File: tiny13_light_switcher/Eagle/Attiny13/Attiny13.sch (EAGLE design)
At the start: 34 parts, among them Q1 2SA1015, Q2 2SC1815, Q3 2SA1015, U1 ATTiny13

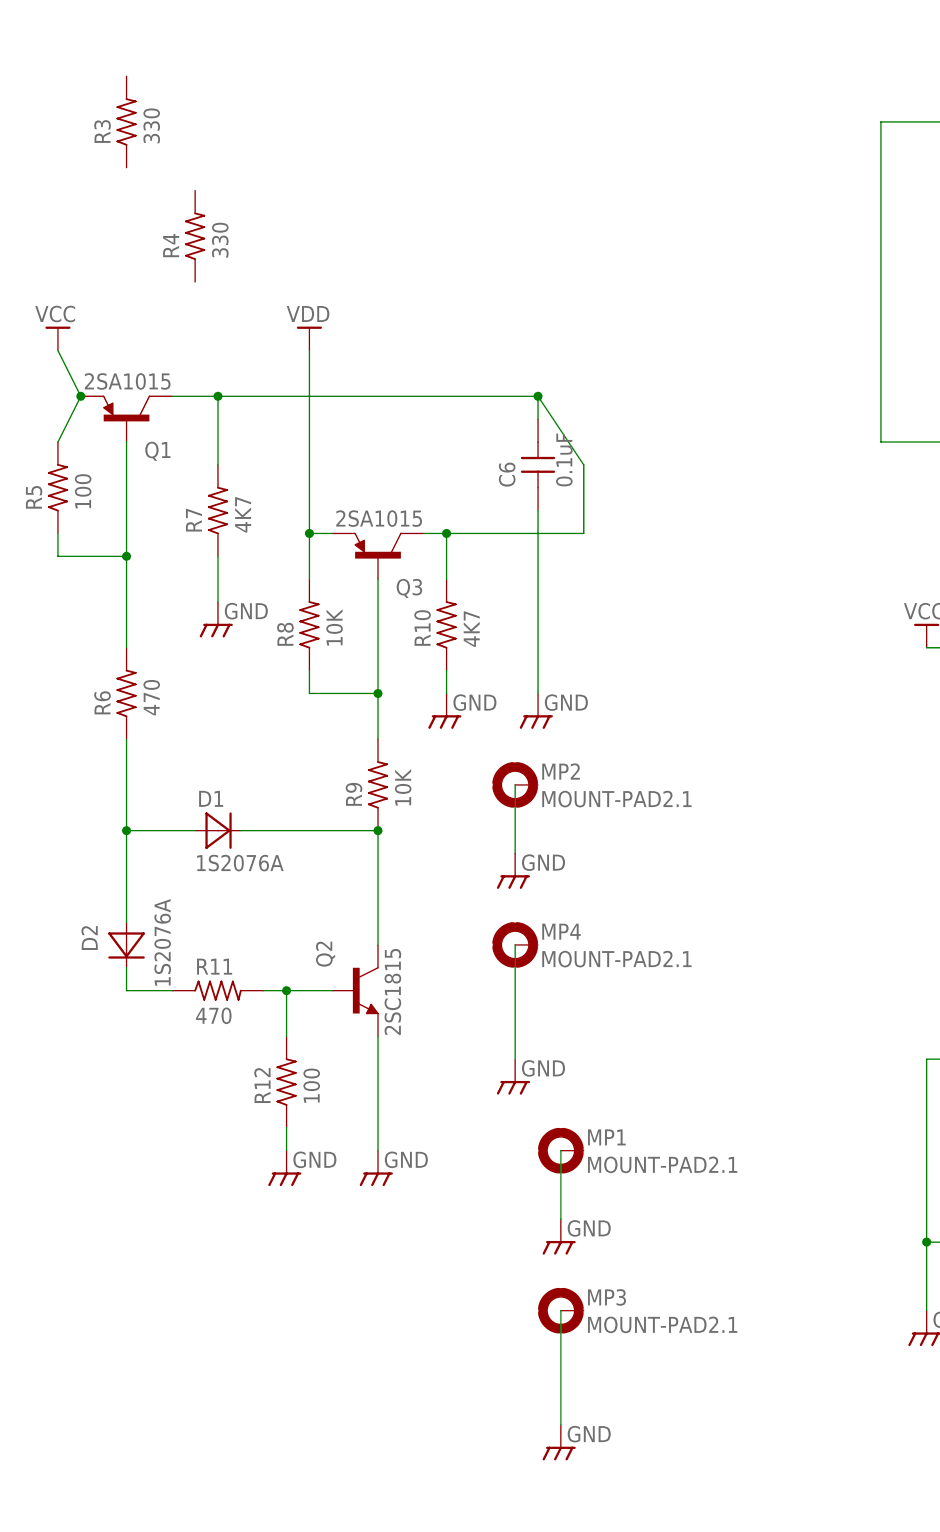
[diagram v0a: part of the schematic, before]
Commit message: Remove no use parts.
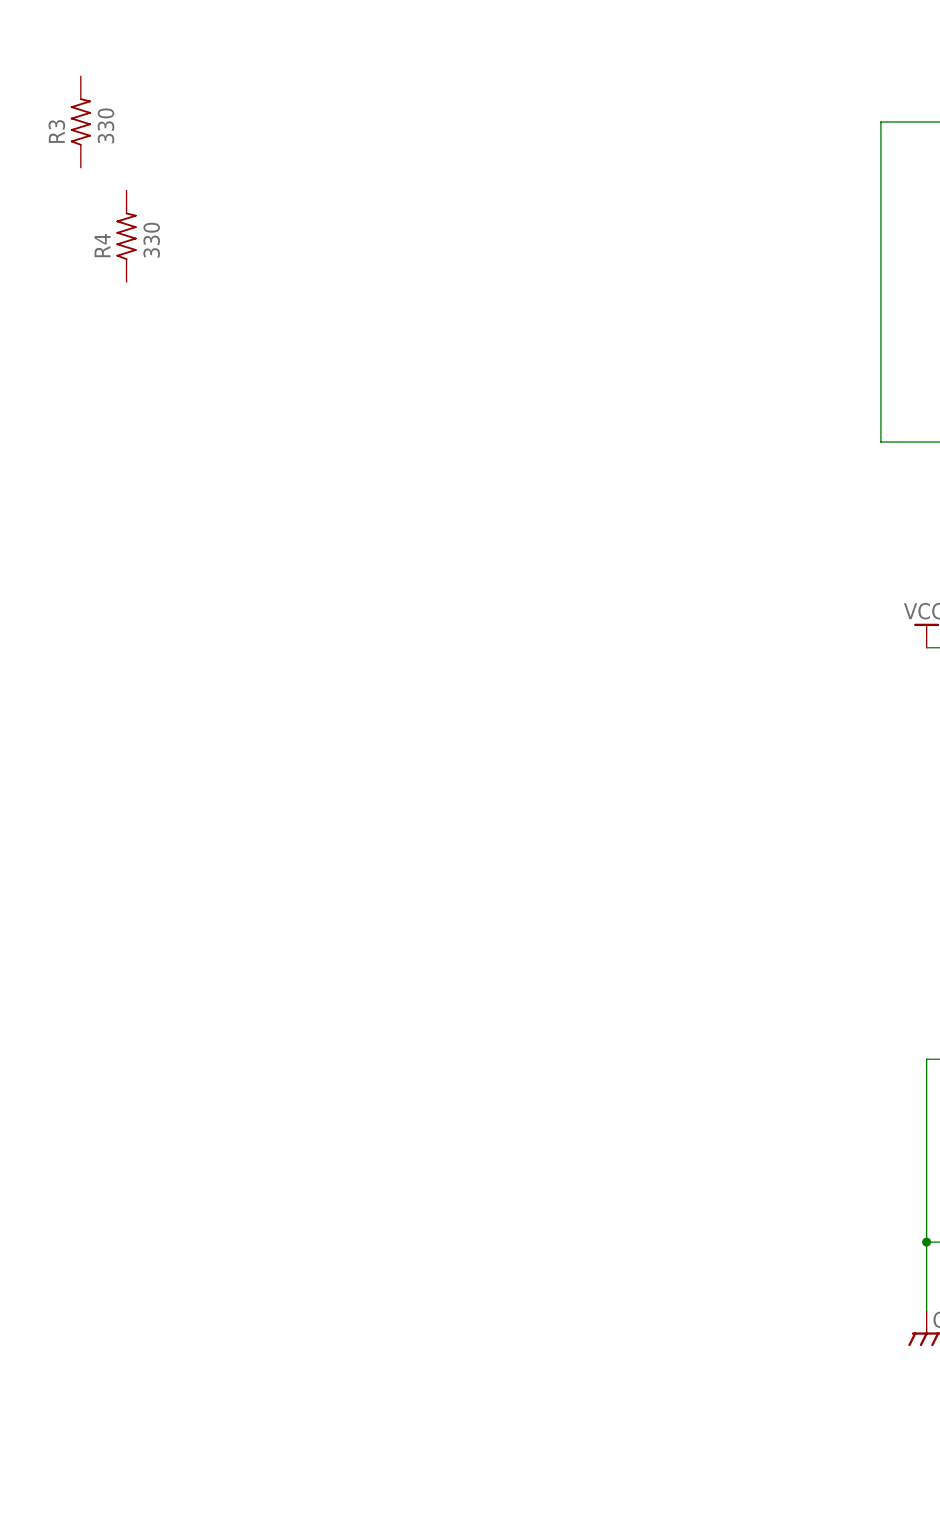
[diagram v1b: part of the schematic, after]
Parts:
- removed C6: 0.1uF, MyLib:CAPDIP_1
- removed D1, D2: 1S2076A, MyLib:DIODEGENERIC_2
- removed MP1, MP2, MP3, MP4: MOUNT-PAD2.1, MyLib:MOUNT-PAD2.1
- removed Q1, Q3: 2SA1015, MyLib:2SA1015
- removed Q2: 2SC1815, MyLib:2SC1815
- removed R10, R7: 4K7, MyLib:R0.125W_3P
- removed R11, R6: 470, MyLib:R0.125W_3P
- removed R12, R5: 100, MyLib:R0.125W_3P
- removed R8, R9: 10K, MyLib:R0.125W_3P
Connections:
- removed net N$11: Q1.B, R5.1, R6.2
- removed net N$13: Q3.B, R8.1, R9.2
- removed net N$14: Q2.B, R11.2, R12.2
- removed net N$15: D1.K, Q2.C, R9.1
- removed net N$16: D2.K, R11.1
- removed net N$17: D1.A, D2.A, R6.1
- removed net N$3: C6.2, Q1.C, Q3.C, R10.2, R7.2
- removed net VDD: Q3.E, R8.2
- net GND: no longer C6.1, MP1.MOUNT, MP2.MOUNT, MP3.MOUNT, MP4.MOUNT, Q2.E, R10.1, R12.1, R7.1
- net VCC: no longer Q1.E, R5.2
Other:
- moved on the sheet: R3, R4

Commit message: Add tiny85 writer.
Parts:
- added C1: 0.1uF, MyLib:CAPDIP_1
- added C2: 4.7uF, MyLib:CAPDIP_1
- added D1: ＳＢＭ１０４５ＶＳＳ, adafruit:SCHOTTKY-DIODEDO41
- added D2, D3: ＧＤＺＪ３．６Ｂ, diode:ZENER-DIODEDO34-7
- added ESDV_L, ESDV_R, ESDV_R2: PINHD-1X10, adafruit:PINHD-1X10
- added J1: USB_A_SMT_MALE, SparkFun-Connectors:USB_A_SMT_MALE
- added JP3: VINSEL, pinhead:PINHD-1X3
- added JP5: (no value), pinhead:PINHD-1X2
- added JP6: VSEL, pinhead:PINHD-1X3
- added JP7: Regulator, pinhead:PINHD-1X5
- added LED8, LED9: (no value), adafruit:LEDSFH480
- added R1: 68R, MyLib:R0.125W_3P
- added R5, R6: (no value), MyLib:R0.125W_3P
- added U2: ATTiny85, atmel:TINY138P3
- Q4, Q5, Q6: value (none) -> 2N7000
- R3: value 330 -> 1K5
- R4: value 330 -> 68R
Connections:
- new net +5V: C1.2, C2.2, ESDV_L.10, JP5.2, JP6.2, LED9.A, U2.VCC
- new net N$1: D1.C, J1.VBUS
- new net N$11: ESDV_R.7, ESDV_R2.7, R1.1, U2.PB4(ADC2/PCINT4)
- new net N$12: ESDV_R.5, ESDV_R2.5, U2.PB5(RESET#/ADC0/DW/PCINT5)
- new net N$13: LED9.C, R5.2
- new net N$14: LED8.C, R6.1
- new net N$15: ESDV_L.6, LED8.A, U2.PB1(MISO/AIN1/OC0B/INT0/PCINT1)
- new net N$16: ESDV_L.5, U2.PB0(MOSI/AIN0/OC0A/PCINT0)
- new net N$17: JP3.2, JP7.1, JP7.4
- new net N$18: ESDV_L.7, U2.PB2(SCK/ADC1/T0/PCINT2)
- new net N$19: D3.C, J1.D+, R1.2
- new net N$20: ESDV_R.10, ESDV_R2.10, JP3.1
- new net N$21: ESDV_R.2, ESDV_R2.2
- new net N$22: ESDV_R.3, ESDV_R2.3
- new net N$23: ESDV_R.4, ESDV_R2.4
- new net N$24: ESDV_R.8, ESDV_R2.8
- new net N$25: ESDV_L.1, JP5.1
- new net N$26: JP6.3, JP7.2, JP7.5
- new net N$3: ESDV_R.6, ESDV_R2.6, R4.1, U2.PB3(ADC3/CLKI/PCINT3)
- new net N$4: D2.C, J1.D-, R3.1, R4.2
- new net VDD: D1.A, JP3.3, JP6.1, R3.2
- net GND: now also C1.1, C2.1, D2.A, D3.A, ESDV_L.9, ESDV_R.1, ESDV_R.9, ESDV_R2.1, ESDV_R2.9, J1.GND, JP7.3, R5.1, R6.2, U2.GND
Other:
- note added: "& Espr Developer Socket"
- note added: "Attiny85 writer"
- moved on the sheet: R3, R4

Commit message: Change sub pin header to wroom02 breakout board.
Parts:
- removed ESDV_R2: PINHD-1X10, adafruit:PINHD-1X10
- removed JP5: (no value), pinhead:PINHD-1X2
- added WR02_L: WR02_L, pinhead:PINHD-1X8
- added WR02_R: WR02_R, pinhead:PINHD-1X8
- JP2: value (none) -> VDD
- LED8: value (none) -> PRG_LED
- LED9: value (none) -> PWR_LED
- R5: value (none) -> R_PWR_LED
- R6: value (none) -> R_PROG_LED
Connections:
- new net N$27: ESDV_R.3, WR02_R.3
- new net N$28: ESDV_R.4, WR02_R.4
- new net N$29: ESDV_R.8, WR02_R.8
- net +5V: now also WR02_L.1; no longer JP5.2
- net GND: now also WR02_R.1; no longer ESDV_R2.1, ESDV_R2.9
- net N$11: now also WR02_R.7; no longer ESDV_R2.7
- net N$12: now also WR02_R.5; no longer ESDV_R2.5
- net N$15: now also WR02_L.6
- net N$16: now also WR02_L.5
- net N$18: now also WR02_L.7
- net N$20: no longer ESDV_R2.10
- net N$21: now also ESDV_L.2, WR02_L.2; no longer ESDV_R.2, ESDV_R2.2
- net N$22: now also ESDV_L.3, WR02_L.3; no longer ESDV_R.3, ESDV_R2.3
- net N$23: now also ESDV_L.4, WR02_L.4; no longer ESDV_R.4, ESDV_R2.4
- net N$24: now also ESDV_L.8, WR02_L.8; no longer ESDV_R.8, ESDV_R2.8
- net N$25: now also ESDV_R.2, WR02_R.2; no longer ESDV_L.1, JP5.1
- net N$3: now also WR02_R.6; no longer ESDV_R2.6
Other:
- moved on the sheet: ESDV_L, LED8

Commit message: Add pattern diagram.
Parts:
- renumbered LED7 to LED2
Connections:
- net N$10: now also LED3.C; no longer LED5.C
- net N$5: now also LED6.C; no longer LED3.C
- net N$9: now also LED5.C; no longer LED6.C
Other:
- moved on the sheet: LED3, LED5, LED6
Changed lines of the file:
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@@
 <part name="VCC4" library="pwr" deviceset="VCC" device=""/>
 <part name="LED1" library="led" deviceset="LED" device="3MM" value="RED"/>
+<part name="LED6" library="led" deviceset="LED" device="3MM" value="RED"/>
+<part name="LED4" library="led" deviceset="LED" device="3MM" value="RED"/>
 <part name="LED3" library="led" deviceset="LED" device="3MM" value="RED"/>
-<part name="LED4" library="led" deviceset="LED" device="3MM" value="RED"/>
 <part name="LED5" library="led" deviceset="LED" device="3MM" value="RED"/>
-<part name="LED6" library="led" deviceset="LED" device="3MM" value="RED"/>
-<part name="LED7" library="led" deviceset="LED" device="3MM" value="RED"/>
+<part name="LED2" library="led" deviceset="LED" device="3MM" value="RED"/>
 <part name="J1" library="SparkFun-Connectors" deviceset="USB_A" device="_SMT_MALE"/>
 <part name="SUPPLY1" library="supply2" library_urn="urn:adsk.eagle:library:372" deviceset="GND" device=""/>
@@
 <instance part="VCC4" gate="VCC" x="119.38" y="106.68"/>
 <instance part="LED1" gate="G$1" x="149.86" y="86.36"/>
-<instance part="LED3" gate="G$1" x="160.02" y="86.36"/>
+<instance part="LED6" gate="G$1" x="160.02" y="86.36"/>
 <instance part="LED4" gate="G$1" x="187.96" y="86.36"/>
-<instance part="LED5" gate="G$1" x="198.12" y="86.36"/>
-<instance part="LED6" gate="G$1" x="231.14" y="86.36"/>
-<instance part="LED7" gate="G$1" x="241.3" y="86.36"/>
+<instance part="LED3" gate="G$1" x="198.12" y="86.36"/>
+<instance part="LED5" gate="G$1" x="231.14" y="86.36"/>
+<instance part="LED2" gate="G$1" x="241.3" y="86.36"/>
 <instance part="J1" gate="G$1" x="53.34" y="152.4" rot="R90"/>
 <instance part="SUPPLY1" gate="GND" x="71.12" y="144.78" rot="R90"/>
@@
 <wire x1="149.86" y1="104.14" x2="160.02" y2="104.14" width="0.1524" layer="91"/>
 <junction x="149.86" y="104.14"/>
-<pinref part="LED3" gate="G$1" pin="A"/>
+<pinref part="LED6" gate="G$1" pin="A"/>
 <wire x1="160.02" y1="104.14" x2="160.02" y2="88.9" width="0.1524" layer="91"/>
 <wire x1="160.02" y1="104.14" x2="187.96" y2="104.14" width="0.1524" layer="91"/>
@@
 <wire x1="187.96" y1="104.14" x2="198.12" y2="104.14" width="0.1524" layer="91"/>
 <junction x="187.96" y="104.14"/>
-<pinref part="LED5" gate="G$1" pin="A"/>
+<pinref part="LED3" gate="G$1" pin="A"/>
 <wire x1="198.12" y1="104.14" x2="198.12" y2="88.9" width="0.1524" layer="91"/>
 <wire x1="198.12" y1="104.14" x2="231.14" y2="104.14" width="0.1524" layer="91"/>
 <junction x="198.12" y="104.14"/>
-<pinref part="LED6" gate="G$1" pin="A"/>
+<pinref part="LED5" gate="G$1" pin="A"/>
 <wire x1="231.14" y1="104.14" x2="231.14" y2="88.9" width="0.1524" layer="91"/>
 <wire x1="231.14" y1="104.14" x2="241.3" y2="104.14" width="0.1524" layer="91"/>
 <junction x="231.14" y="104.14"/>
-<pinref part="LED7" gate="G$1" pin="A"/>
+<pinref part="LED2" gate="G$1" pin="A"/>
 <wire x1="241.3" y1="104.14" x2="241.3" y2="88.9" width="0.1524" layer="91"/>
 </segment>
@@
 <net name="N$5" class="0">
 <segment>
-<pinref part="LED3" gate="G$1" pin="C"/>
+<pinref part="LED6" gate="G$1" pin="C"/>
 <wire x1="160.02" y1="81.28" x2="160.02" y2="73.66" width="0.1524" layer="91"/>
 <pinref part="Q6" gate="G$1" pin="D"/>
@@
 <wire x1="187.96" y1="81.28" x2="187.96" y2="73.66" width="0.1524" layer="91"/>
 <wire x1="187.96" y1="73.66" x2="198.12" y2="73.66" width="0.1524" layer="91"/>
-<pinref part="LED5" gate="G$1" pin="C"/>
+<pinref part="LED3" gate="G$1" pin="C"/>
 <wire x1="198.12" y1="73.66" x2="198.12" y2="81.28" width="0.1524" layer="91"/>
 <wire x1="198.12" y1="73.66" x2="198.12" y2="58.42" width="0.1524" layer="91"/>
@@
 <net name="N$9" class="0">
 <segment>
-<pinref part="LED7" gate="G$1" pin="C"/>
+<pinref part="LED2" gate="G$1" pin="C"/>
 <wire x1="241.3" y1="81.28" x2="241.3" y2="73.66" width="0.1524" layer="91"/>
 <pinref part="Q4" gate="G$1" pin="D"/>
 <wire x1="241.3" y1="73.66" x2="241.3" y2="60.96" width="0.1524" layer="91"/>
 <wire x1="241.3" y1="60.96" x2="233.68" y2="60.96" width="0.1524" layer="91"/>
-<pinref part="LED6" gate="G$1" pin="C"/>
+<pinref part="LED5" gate="G$1" pin="C"/>
 <wire x1="231.14" y1="81.28" x2="231.14" y2="73.66" width="0.1524" layer="91"/>
 <wire x1="231.14" y1="73.66" x2="241.3" y2="73.66" width="0.1524" layer="91"/>

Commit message: Change USB connector.
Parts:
- removed J1: USB_A_SMT_MALE, SparkFun-Connectors:USB_A_SMT_MALE
- added J2: USB_A_PTH_MALE, SparkFun-Connectors:USB_A_PTH_MALE
- JP2: value VDD -> PWR_SPLY
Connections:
- new net AGND: C1.1, C2.1, D2.A, D3.A, ESDV_L.9, ESDV_R.1, ESDV_R.9, J2.GND, JP7.3, R5.1, R6.2, U2.GND, WR02_R.1
- net GND: no longer C1.1, C2.1, D2.A, D3.A, ESDV_L.9, ESDV_R.1, ESDV_R.9, J1.GND, JP7.3, R5.1, R6.2, U2.GND, WR02_R.1
- net N$1: now also J2.VBUS; no longer J1.VBUS
- net N$19: now also J2.D+; no longer J1.D+
- net N$4: now also J2.D-; no longer J1.D-
